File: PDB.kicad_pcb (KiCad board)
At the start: 2 copper layers, 50 x 90 mm, 67 parts, among them J1 Conn_02x03_Odd_Even, J2 USB_C_Receptacle_USB2.0, J3 Conn_01x02, J4 Conn_01x02, J5 Conn_01x02, J6 Conn_01x02, J7 Conn_01x02_MountingPin, SW1 SW_Push, U1 ATmega2560-16AU, U2 LMZ13608, U3 LTC2946, U4 LTC2946, U5 FT230XQ, U6 Si8621, Y1 16MHz

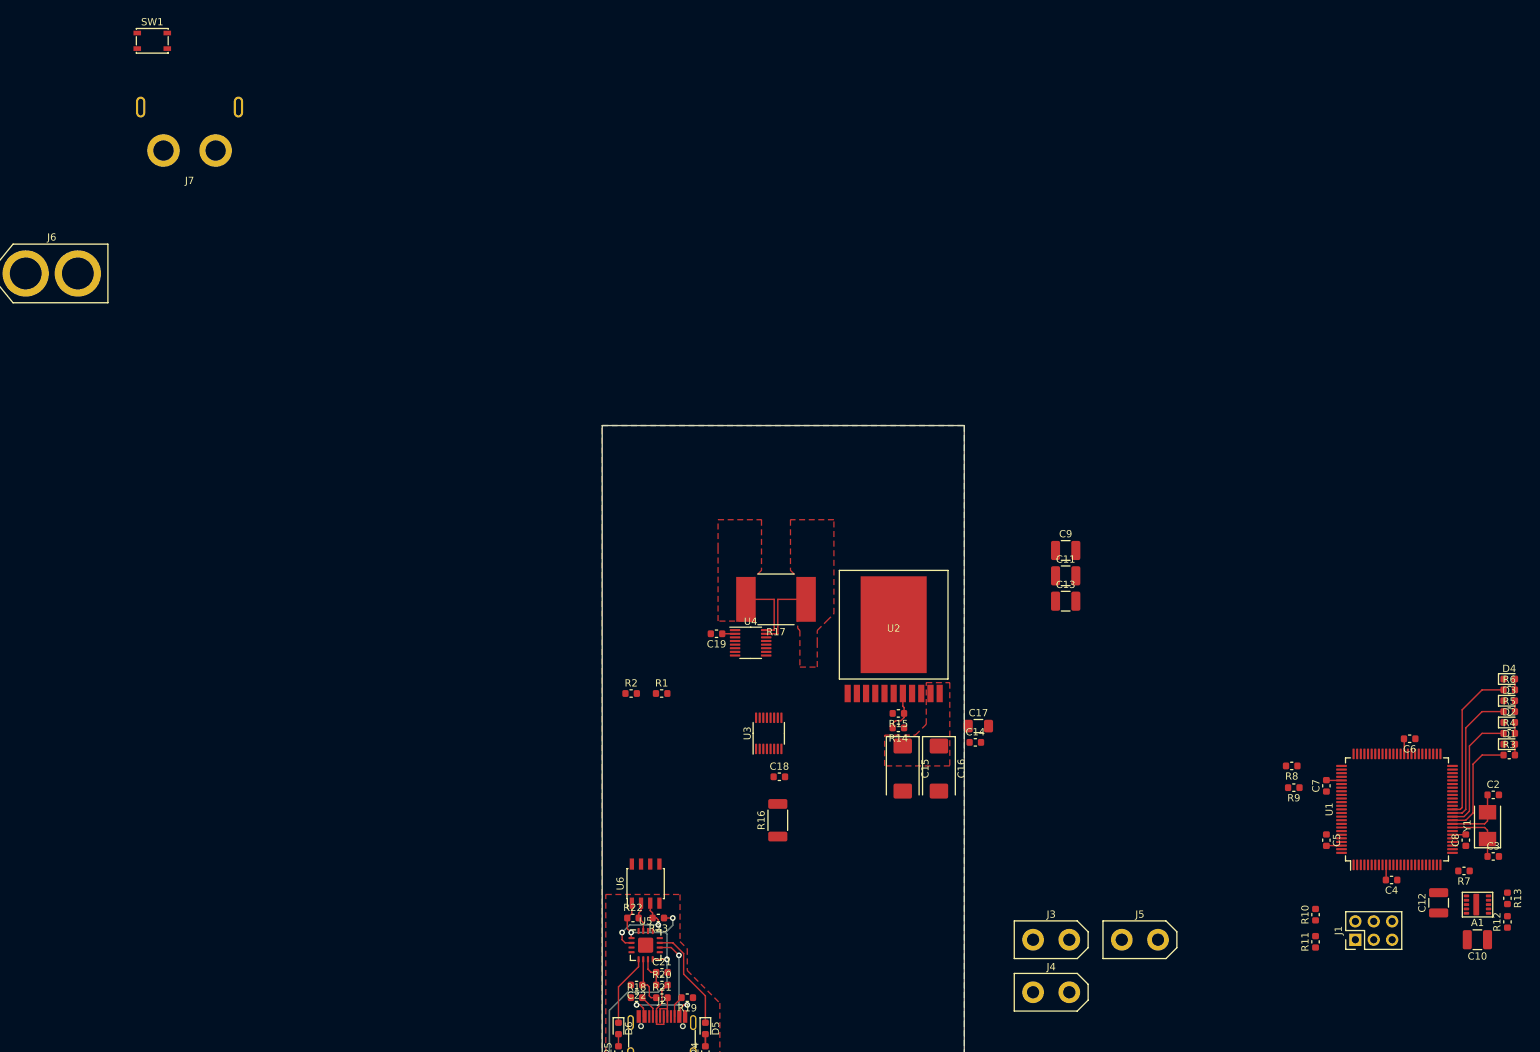
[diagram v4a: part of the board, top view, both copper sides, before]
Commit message: LMZM23600 from kicad libs
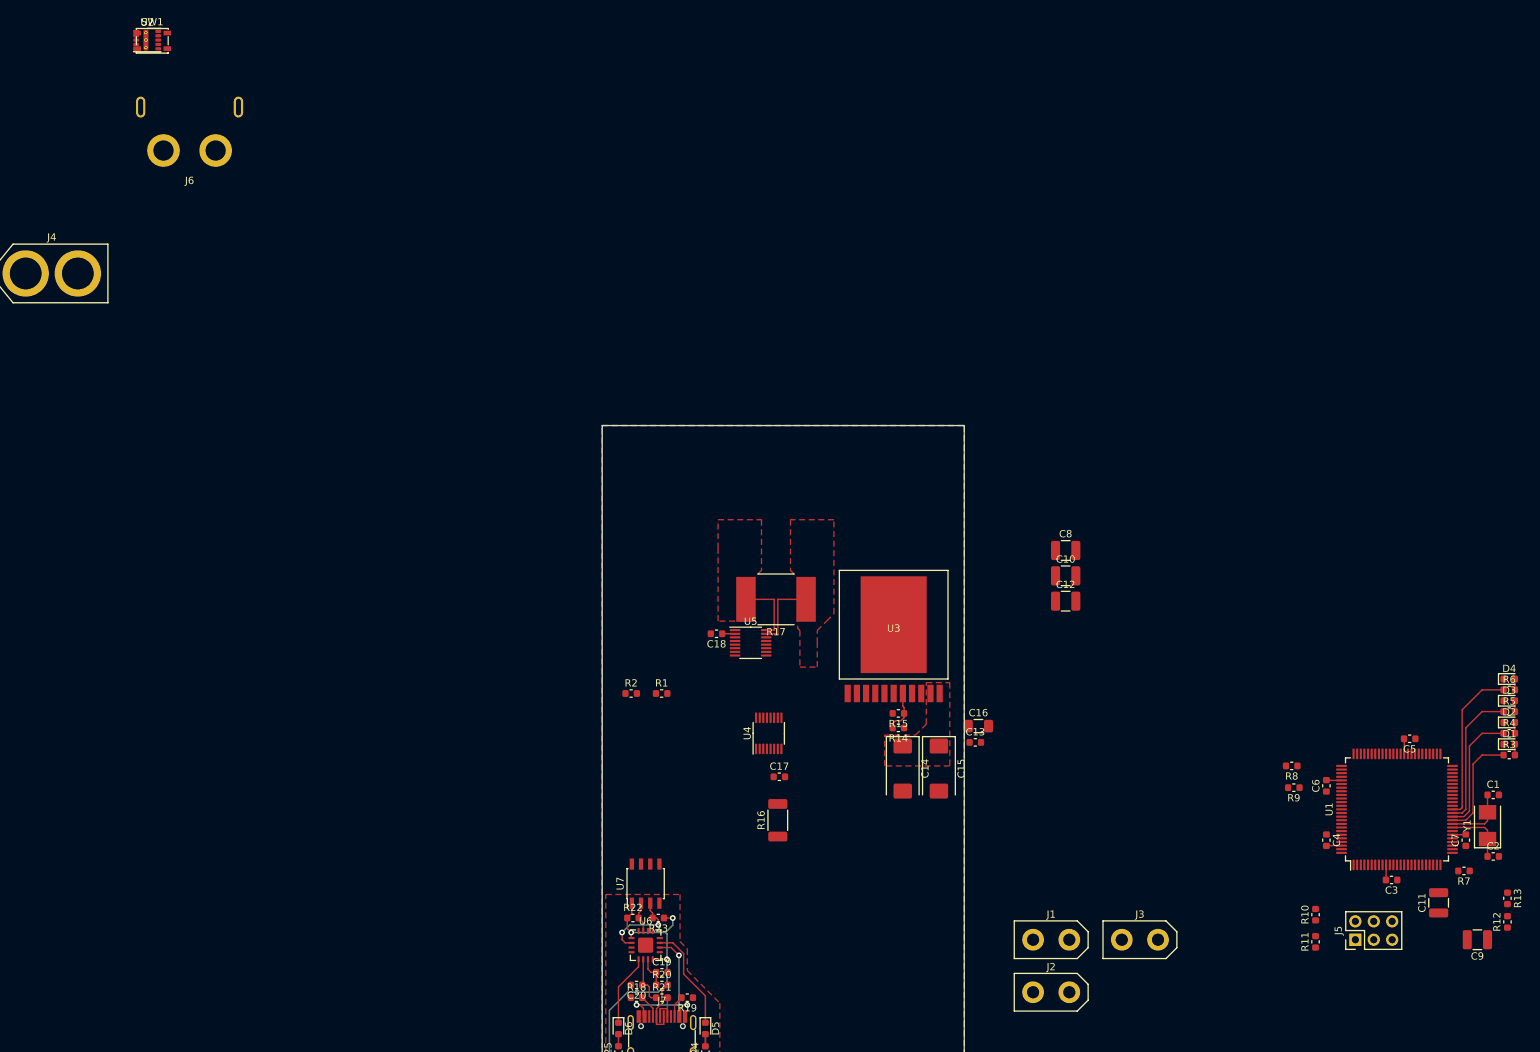
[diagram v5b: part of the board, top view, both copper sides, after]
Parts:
- removed A1: lmzm23600, LMZM23600:lmzm23600
- added U2: LMZM23600, Package_LGA:Texas_SIL0010A_MicroSiP-10-1EP_3.8x3mm_P0.6mm_EP0.7x2.9mm_ThermalVias, F.Cu at (2.18, 1.78)
- renumbered C2 to C1, C11 to C10, C12 to C11, C13 to C12, C14 to C13, C15 to C14, C16 to C15, C17 to C16, C18 to C17, C19 to C18, C21 to C19, C3 to C2, C22 to C20, C4 to C3, C5 to C4, C6 to C5, C7 to C6, C8 to C7, C9 to C8, C10 to C9, J3 to J1, J4 to J2, J5 to J3, J6 to J4, J1 to J5, J7 to J6, J2 to J7, U2 to U3, U3 to U4, U4 to U5, U5 to U6, U6 to U7
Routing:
- added copper zone on F.Cu, net (none)
- removed copper zone on F.Cu, net Net-(C13-Pad1)

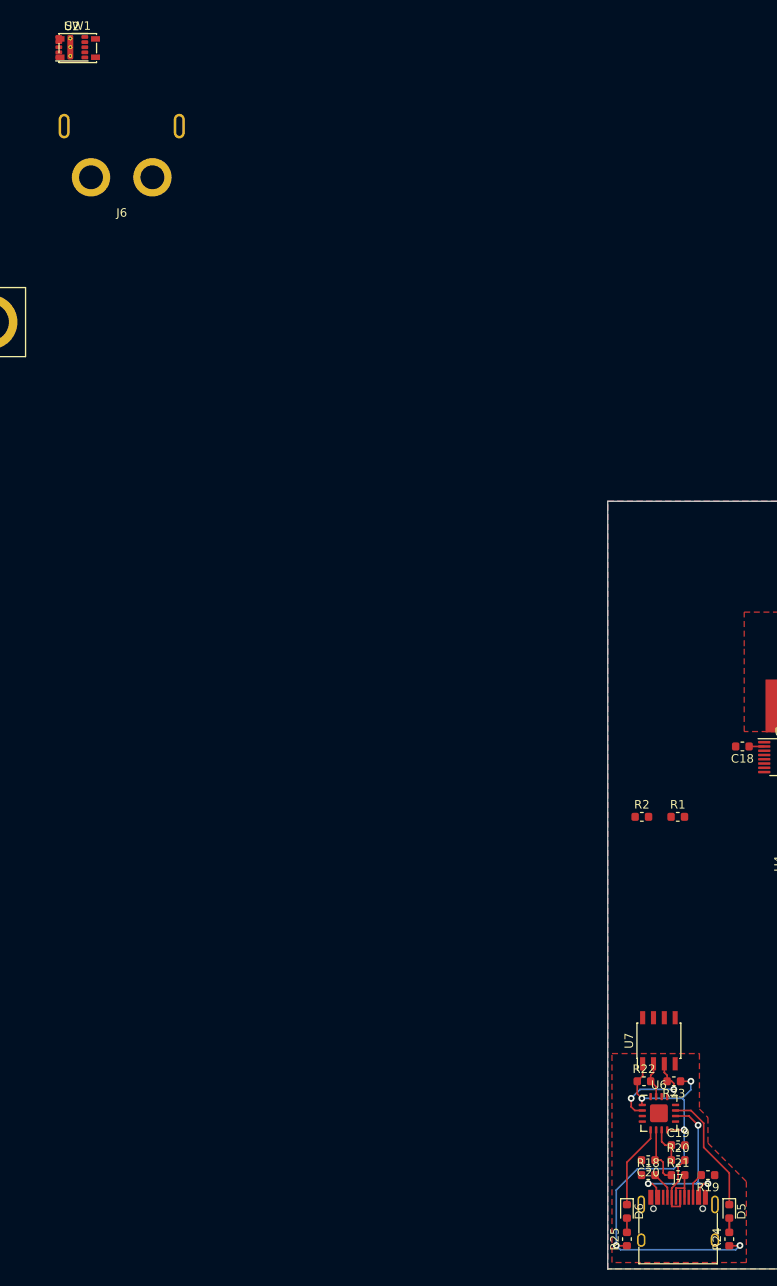
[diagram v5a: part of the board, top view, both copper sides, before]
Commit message: remove isolation from FT230
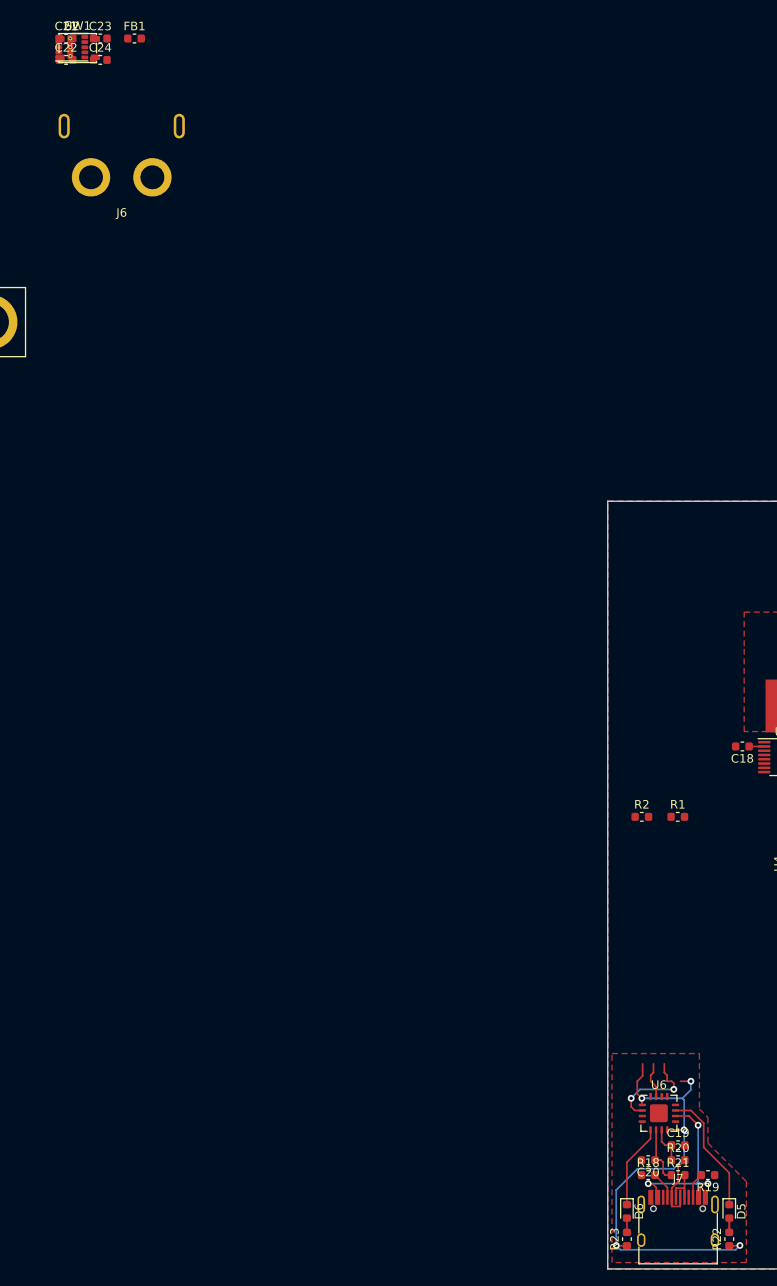
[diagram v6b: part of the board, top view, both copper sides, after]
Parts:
- removed the R22 at (69.2, 123.0)
- removed the R23 at (72.8, 123.0)
- removed U7: Si8621, Package_SO:SOIC-8_3.9x4.9mm_P1.27mm
- added C21: 10nF, Capacitor_SMD:C_0603_1608Metric, F.Cu at (1.51, 0.76)
- added C22: 100nF, Capacitor_SMD:C_0603_1608Metric, F.Cu at (1.51, 3.27)
- added C23: 4.7µF, Capacitor_SMD:C_0603_1608Metric, F.Cu at (5.52, 0.76)
- added C24: 100nF, Capacitor_SMD:C_0603_1608Metric, F.Cu at (5.52, 3.27)
- added FB1: 600 Ohms @ 100MHz, Capacitor_SMD:C_0603_1608Metric, F.Cu at (9.53, 0.76)
- renumbered R24 to R22, R25 to R23
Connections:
- J7 pad A4: Net-(J7-PadA4) -> VBUS
- J7 pad A6: Net-(J7-PadA6) -> Net-(C20-Pad1)
- J7 pad A7: Net-(J7-PadA7) -> Net-(C19-Pad1)
- J7 pad A9: Net-(J7-PadA4) -> VBUS
- J7 pad B4: Net-(J7-PadA4) -> VBUS
- J7 pad B6: Net-(J7-PadA6) -> Net-(C20-Pad1)
- J7 pad B7: Net-(J7-PadA7) -> Net-(C19-Pad1)
- J7 pad B9: Net-(J7-PadA4) -> VBUS
- R20 pad 1: Net-(C19-Pad1) -> Net-(R20-Pad1)
- R20 pad 2: Net-(J7-PadA7) -> Net-(C19-Pad1)
- R21 pad 1: Net-(C20-Pad1) -> Net-(R21-Pad1)
- R21 pad 2: Net-(J7-PadA6) -> Net-(C20-Pad1)
- R22 pad 1: Net-(R22-Pad1) -> Net-(C24-Pad1)
- R23 pad 1: Net-(R22-Pad1) -> Net-(C24-Pad1)
- U6 pad 1: Net-(R22-Pad1) -> Net-(C24-Pad1)
- U6 pad 10: Net-(J7-PadA4) -> /FT230/5VOUT
- U6 pad 15: Net-(R22-Pad2) -> /RX
- U6 pad 2: Net-(R23-Pad2) -> /TX
- U6 pad 6: Net-(C20-Pad1) -> Net-(R21-Pad1)
- U6 pad 7: Net-(C19-Pad1) -> Net-(R20-Pad1)
- U6 pad 8: Net-(R22-Pad1) -> Net-(C24-Pad1)
- U6 pad 9: (no net) -> Net-(C24-Pad1)
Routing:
- net Net-(R22-Pad1): track 56.2 -> 0.00 mm, vias 5 -> 0
- net Net-(C24-Pad1): track 0.00 -> 56.2 mm, vias 0 -> 5
- net Net-(R23-Pad2): track 11.7 -> 0.00 mm, vias 2 -> 0
- net /TX: track 0.00 -> 11.7 mm, vias 0 -> 2
- net Net-(J7-PadA7): track 8.14 -> 0.00 mm
- net Net-(C19-Pad1): track 4.44 -> 12.6 mm
- net Net-(C20-Pad1): track 6.99 -> 11.7 mm
- net Net-(J7-PadA6): track 4.69 -> 0.00 mm
- net Net-(R22-Pad2): track 4.25 -> 0.00 mm
- net /RX: track 0.00 -> 4.25 mm

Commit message: more LEDs
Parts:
- added D5: , LED_SMD:LED_0603_1608Metric, F.Cu at (1.55, 0.80)
- added D6: , LED_SMD:LED_0603_1608Metric, F.Cu at (1.55, 3.39)
- added D7: , LED_SMD:LED_0603_1608Metric, F.Cu at (5.60, 0.80)
- added D8: , LED_SMD:LED_0603_1608Metric, F.Cu at (1.55, 5.98)
- added R10: 5.6, Resistor_SMD:R_0603_1608Metric, F.Cu at (9.57, 3.35)
- added R7: 5.6, Resistor_SMD:R_0603_1608Metric, F.Cu at (5.56, 3.35)
- added R8: 5.6, Resistor_SMD:R_0603_1608Metric, F.Cu at (9.61, 0.76)
- added R9: 5.6, Resistor_SMD:R_0603_1608Metric, F.Cu at (5.56, 5.86)
- renumbered D6 to D10, D5 to D9, R7 to R11, R8 to R12, R9 to R13, R10 to R14, R11 to R15, R12 to R16, R13 to R17, R14 to R18, R15 to R19, R16 to R20, R17 to R21, R18 to R22, R19 to R23, R20 to R24, R21 to R25, R22 to R26, R23 to R27
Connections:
- U1 pad 39: (no net) -> Net-(R7-Pad1)
- U1 pad 40: (no net) -> Net-(R8-Pad1)
- U1 pad 41: (no net) -> Net-(R9-Pad1)
- U1 pad 42: (no net) -> Net-(R10-Pad1)

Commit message: layout
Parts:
- added H1: MountingHole, MountingHole:MountingHole_3.2mm_M3, F.Cu at (70.0, 130.0)
- added H2: MountingHole, MountingHole:MountingHole_3.2mm_M3, F.Cu at (110.0, 130.0)
- added H3: MountingHole, MountingHole:MountingHole_3.2mm_M3, F.Cu at (110.0, 95.0)
- added H4: MountingHole, MountingHole:MountingHole_3.2mm_M3, F.Cu at (110.0, 75.0)
- added H5: MountingHole, MountingHole:MountingHole_3.2mm_M3, F.Cu at (70.0, 75.0)
- added H6: MountingHole, MountingHole:MountingHole_3.2mm_M3, F.Cu at (70.0, 95.0)
- added J11: USB_C_Receptacle_USB2.0, GT-USB-7010:USB_C_Receptacle_GT-USB-7010, F.Cu at (82.0, 131.0)
- added J4: Conn_01x02, XT30:XT30PB-F, F.Cu at (88.0, 61.5)
- added J5: Conn_01x02, XT30:XT30PB-F, F.Cu at (94.5, 61.5)
- added J6: Conn_01x02, Connector_PinHeader_2.54mm:PinHeader_1x02_P2.54mm_Vertical, F.Cu at (69.0, 69.5)
- J7: value USB_C_Receptacle_USB2.0 -> Conn_01x02; footprint GT-USB-7010:USB_C_Receptacle_GT-USB-7010 -> Connector_PinHeader_2.54mm:PinHeader_1x02_P2.54mm_Vertical
- moved SW1 211.1 mm to (172.5, 127.5)
- moved D5 163.8 mm to (99.0, 132.5), turned to 90 degrees
- moved D7 163.5 mm to (102.5, 132.5), turned to 90 degrees
- moved D8 163.0 mm to (104.2, 132.5), turned to 90 degrees
- moved D6 162.8 mm to (100.8, 132.5), turned to 90 degrees
- moved R8 157.5 mm to (100.8, 129.2), turned to 270 degrees
- moved R10 157.5 mm to (104.2, 129.2), turned to 270 degrees
- moved R9 156.9 mm to (102.5, 129.2), turned to 270 degrees
- moved R7 156.8 mm to (99.0, 129.2), turned to 270 degrees
- moved C21 150.0 mm to (87.8, 123.5)
- moved C23 146.3 mm to (87.8, 121.8)
- moved C22 145.1 mm to (87.8, 120.0)
- moved FB1 143.6 mm to (85.2, 122.7), turned to 270 degrees
- moved C24 141.0 mm to (85.2, 119.5), turned to 270 degrees
- moved U2 134.4 mm to (101.8, 92.0), turned to 270 degrees
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- renumbered J6 to J10, J4 to J8, J5 to J9
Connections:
- C10 pad 1: /BAT/VBATOUT -> +BATT
- C11 pad 1: /BAT/VBATOUT -> +BATT
- C12 pad 1: /BAT/VBATOUT -> +BATT
- C8 pad 1: /BAT/VBATOUT -> +BATT
- J10 pad 2: /BAT/VBATOUT -> +BATT
- J10 pad MP: Net-(J6-PadMP) -> GND
- R21 pad 1: /BAT/VBATOUT -> +BATT
- R22 pad 2: Net-(J7-PadA5) -> Net-(J11-PadA5)
- R23 pad 2: Net-(J7-PadB5) -> Net-(J11-PadB5)
- U2 pad 1: Net-(U2-Pad1) -> GND
- U2 pad 11: Net-(U2-Pad1) -> GND
- U2 pad 3: /BAT/VBATOUT -> +BATT
- U2 pad 4: /BAT/VBATOUT -> +BATT
- U3 pad 1: /BAT/VBATOUT -> +BATT
- U3 pad 2: /BAT/VBATOUT -> +BATT
- U4 pad 1: /BAT/VBATOUT -> +BATT
- U5 pad 1: /BAT/VBATOUT -> +BATT
- U5 pad 15: /BAT/VBATOUT -> +BATT
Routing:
- net +BATT: track 0.00 -> 49.3 mm, vias 0 -> 5
- net GND: track 0.00 -> 43.2 mm, vias 0 -> 21
- net +5V: track 0.00 -> 35.2 mm
- net Net-(J7-PadA4): track 21.9 -> 0.00 mm, vias 3 -> 0
- net /RX: track 4.25 -> 19.0 mm
- net Net-(C13-Pad1): track 0.00 -> 13.6 mm
- net VBUS: track 0.00 -> 13.5 mm
- net Net-(R7-Pad1): track 0.00 -> 10.7 mm, vias 0 -> 2
- net Net-(C24-Pad1): track 56.2 -> 45.8 mm, vias 5 -> 4
- net /BAT/VBATOUT: track 10.2 -> 0.00 mm
- net Net-(R6-Pad1): track 21.8 -> 11.6 mm, vias 0 -> 2
- net Net-(R8-Pad1): track 0.00 -> 10.1 mm, vias 0 -> 2
- net Net-(C17-Pad1): track 0.00 -> 10.0 mm, vias 0 -> 2
- net Net-(R9-Pad1): track 0.00 -> 9.63 mm, vias 0 -> 2
- net /FT230/5VOUT: track 0.00 -> 9.45 mm
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- added copper zone on F.Cu, net +3V3
- added copper zone on F.Cu, net +5V
- added copper zone on F.Cu, net +BATT
- added copper zone on F.Cu, net Net-(C13-Pad1)
- removed copper zone on F.Cu, net (none)
- removed copper zone on F.Cu, net /BAT/VBATOUT
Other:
- board size 50 x 90 mm -> 50 x 80 mm
- net class Default: clearance 0.1 -> 0.15
- rule trace_clearance: 0.1 -> 0.15
- rule via_min_drill: 0.2 -> 0.25
- rule via_min_size: 0.45 -> 0.5
- board text added: "Todo: Not use min size Vias Adhere to design rules + safety margin"
